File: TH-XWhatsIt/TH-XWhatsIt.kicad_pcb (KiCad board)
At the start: 2 copper layers, 145.3 x 129.6 mm, 32 parts, among them J1 MODEL F, J2 EXPANSION, J3 EXPANSION HEADER, J4 EXPANSION BEAMSPRING, J5 BEAMSPRING CONNECTOR, J6 EXPANSION BEAMSPRING, J7 EXPANSION DISPLAYWRITER, J8 DISPLAYWRITER CONNECTOR, J9 EXPANSION DISPLAYWRITER, U1 MCP4921-EP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

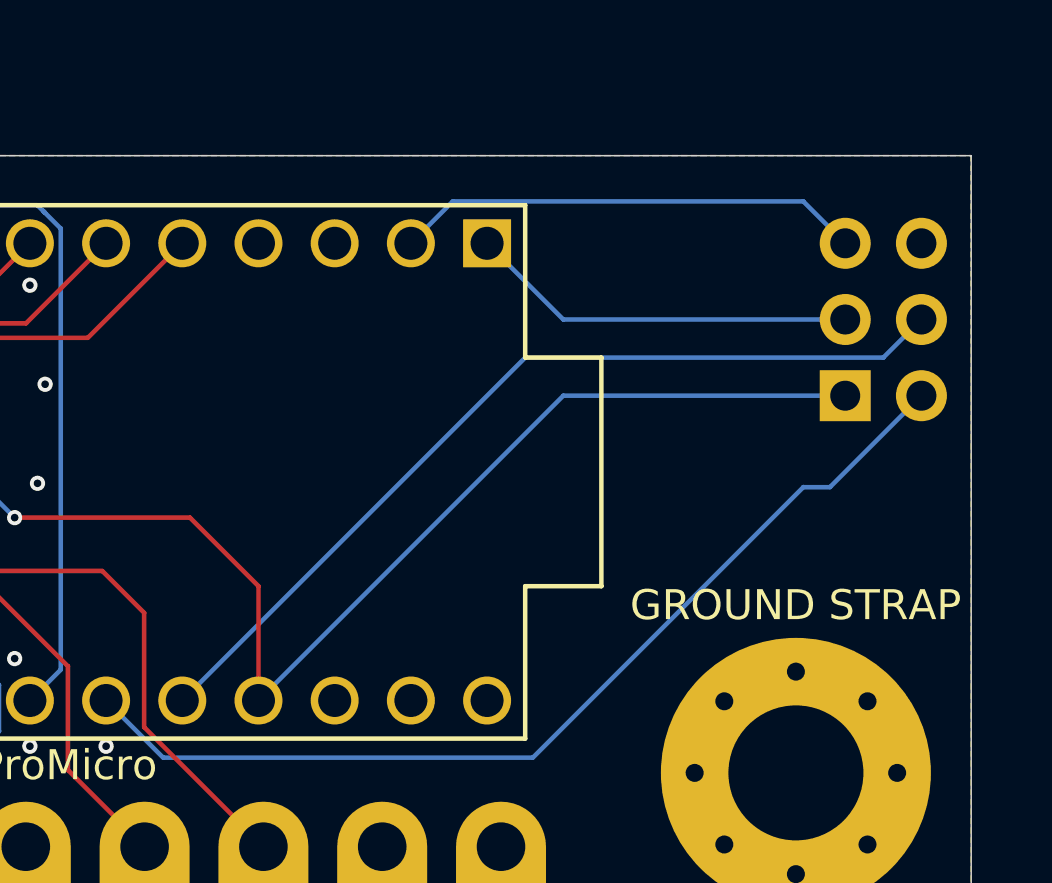
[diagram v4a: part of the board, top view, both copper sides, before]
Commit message: Added pads for easily shorting reset with a screwdriver
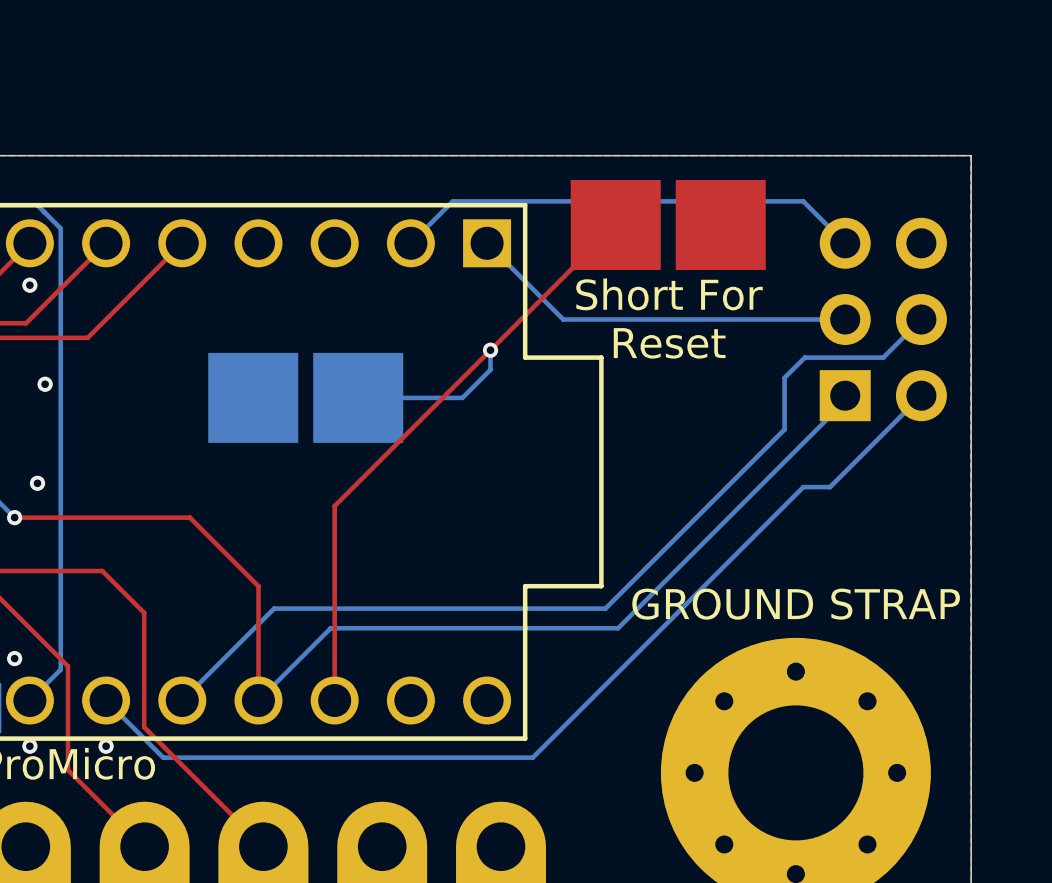
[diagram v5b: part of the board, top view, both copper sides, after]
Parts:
- added SW1: SW_Push, TH-XWhatsIt:PadsToShort, F.Cu at (165.9, 127.8)
- added SW2: SW_Push, TH-XWhatsIt:PadsToShort, B.Cu at (153.8, 133.6)
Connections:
- U5 pad 22: Net-(U5-Pad22) -> RST
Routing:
- net RST: track 0.00 -> 25.2 mm, vias 0 -> 1
- net HEADER4: track 29.9 -> 30.9 mm
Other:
- board text added: "Short For Reset"
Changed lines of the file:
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@@
   (general
     (thickness 1.6)
-    (drawings 31)
-    (tracks 1460)
+    (drawings 33)
+    (tracks 1473)
     (zones 0)
-    (modules 32)
+    (modules 34)
     (nets 132)
   )
@@
   )
   (layers
-    (0 F.Cu signal)
+    (0 F.Cu signal hide)
     (31 B.Cu signal)
     (32 B.Adhes user hide)
@@
     (34 B.Paste user hide)
     (35 F.Paste user hide)
-    (36 B.SilkS user hide)
-    (37 F.SilkS user)
+    (36 B.SilkS user)
+    (37 F.SilkS user hide)
     (38 B.Mask user hide)
     (39 F.Mask user hide)
@@
   (net 127 "Net-(J9-Pad3)")
   (net 128 "Net-(U5-Pad24)")
-  (net 129 "Net-(U5-Pad22)")
-  (net 130 "Net-(U7-Pad9)")
-  (net 131 "Net-(J4-Pad28)")
+  (net 129 "Net-(U7-Pad9)")
+  (net 130 "Net-(J4-Pad28)")
+  (net 131 RST)
   (net_class Default "This is the default net class."
     (clearance 0.1524)
@@
     (add_net "Net-(J9-Pad9)")
     (add_net "Net-(R4-Pad2)")
-    (add_net "Net-(U5-Pad22)")
     (add_net "Net-(U5-Pad24)")
     (add_net "Net-(U7-Pad9)")
@@
     (add_net ROW7)
     (add_net ROW8)
+    (add_net RST)
     (add_net SENSE1)
     (add_net SENSE2)
@@
     (add_net ~SELECTDAC)
   )
+  (module TH-XWhatsIt:PadsToShort (layer B.Cu)
+    (at 153.8478 133.5913 180)
+    (fp_text reference SW2 (at 0 -0.5) (layer B.SilkS) hide
+      (effects (font (size 1 1) (thickness 0.15)) (justify mirror))
+    )
+    (fp_text value SW_Push (at 0 0.5) (layer B.Fab) hide
+      (effects (font (size 1 1) (thickness 0.15)) (justify mirror))
+    )
+    (pad 2 smd rect (at 1.75 -2.88 180) (size 3 3) (layers B.Cu B.Paste B.Mask)
+      (net 48 GNDA))
+    (pad 1 smd rect (at -1.75 -2.88 180) (size 3 3) (layers B.Cu B.Paste B.Mask)
+      (net 131 RST))
+  )
+  (module TH-XWhatsIt:PadsToShort (layer F.Cu)
+    (at 165.93058 127.82804)
+    (fp_text reference SW1 (at -0.0381 5.37972) (layer F.SilkS) hide
+      (effects (font (size 1 1) (thickness 0.15)))
+    )
+    (fp_text value SW_Push (at 0 -0.5) (layer F.Fab)
+      (effects (font (size 1 1) (thickness 0.15)))
+    )
+    (pad 2 smd rect (at 1.75 2.88) (size 3 3) (layers F.Cu F.Paste F.Mask)
+      (net 48 GNDA))
+    (pad 1 smd rect (at -1.75 2.88) (size 3 3) (layers F.Cu F.Paste F.Mask)
+      (net 131 RST))
+  )
   (module Resistor_SMD:R_Array_Convex_4x0603 (layer F.Cu)
     (at 59.436 146.304 270)
@@
       (effects (font (size 1 1) (thickness 0.15)))
     )
-    (fp_text user %R (at 0 0) (layer F.Fab)
-      (effects (font (size 0.5 0.5) (thickness 0.075)))
-    )
     (fp_line (start -0.8 -1.6) (end 0.8 -1.6) (layer F.Fab) (width 0.1))
     (fp_line (start 0.8 -1.6) (end 0.8 1.6) (layer F.Fab) (width 0.1))
@@
     (fp_line (start 1.55 1.85) (end 1.55 -1.85) (layer F.CrtYd) (width 0.05))
     (fp_line (start 1.55 1.85) (end -1.55 1.85) (layer F.CrtYd) (width 0.05))
+    (fp_text user %R (at 0 0) (layer F.Fab)
+      (effects (font (size 0.5 0.5) (thickness 0.075)))
+    )
     (pad 5 smd rect (at 0.9 1.2 270) (size 0.8 0.5) (layers F.Cu F.Paste F.Mask)
       (net 24 SENSE1))
@@
       (effects (font (size 1 1) (thickness 0.15)))
     )
-    (fp_text user %R (at 0 0) (layer F.Fab)
-      (effects (font (size 0.5 0.5) (thickness 0.075)))
-    )
     (fp_line (start -0.8 -1.6) (end 0.8 -1.6) (layer F.Fab) (width 0.1))
     (fp_line (start 0.8 -1.6) (end 0.8 1.6) (layer F.Fab) (width 0.1))
@@
     (fp_line (start 1.55 1.85) (end 1.55 -1.85) (layer F.CrtYd) (width 0.05))
     (fp_line (start 1.55 1.85) (end -1.55 1.85) (layer F.CrtYd) (width 0.05))
+    (fp_text user %R (at 0 0) (layer F.Fab)
+      (effects (font (size 0.5 0.5) (thickness 0.075)))
+    )
     (pad 5 smd rect (at 0.9 1.2 270) (size 0.8 0.5) (layers F.Cu F.Paste F.Mask)
       (net 28 SENSE5))
@@
       (net 48 GNDA))
     (pad 22 thru_hole circle (at -8.89 -7.62 180) (size 1.6 1.6) (drill 1.1) (layers *.Cu *.Mask F.SilkS)
-      (net 129 "Net-(U5-Pad22)"))
+      (net 131 RST))
     (pad 21 thru_hole circle (at -6.35 -7.62 180) (size 1.6 1.6) (drill 1.1) (layers *.Cu *.Mask F.SilkS)
       (net 49 +5VA))
@@
       (net 50 "/beamspring plugboard/BSGROUND"))
     (pad 28 thru_hole oval (at 49.5 -2.54) (size 3 5.5) (drill 1.62 (offset 0 1.25)) (layers *.Cu *.Mask)
-      (net 131 "Net-(J4-Pad28)"))
+      (net 130 "Net-(J4-Pad28)"))
     (pad 27 thru_hole oval (at 45.54 -2.54) (size 3 5.5) (drill 1.62 (offset 0 1.25)) (layers *.Cu *.Mask)
       (net 59 "/beamspring plugboard/BSCOL15"))
@@
       (net 50 "/beamspring plugboard/BSGROUND"))
     (pad 28 thru_hole circle (at 49.5 0) (size 3 3) (drill 1.6) (layers *.Cu *.Mask)
-      (net 131 "Net-(J4-Pad28)"))
+      (net 130 "Net-(J4-Pad28)"))
     (pad 27 thru_hole circle (at 45.54 0) (size 3 3) (drill 1.6) (layers *.Cu *.Mask)
       (net 59 "/beamspring plugboard/BSCOL15"))
@@
       (net 49 +5VA))
     (pad 9 smd roundrect (at 2.475 4.445 90) (size 1.95 0.6) (layers F.Cu F.Paste F.Mask) (roundrect_rratio 0.25)
-      (net 130 "Net-(U7-Pad9)"))
+      (net 129 "Net-(U7-Pad9)"))
     (pad 8 smd roundrect (at -2.475 4.445 90) (size 1.95 0.6) (layers F.Cu F.Paste F.Mask) (roundrect_rratio 0.25)
       (net 48 GNDA))
@@
     )
   )
+  (gr_text "Short For\nReset" (at 153.75636 140.20546) (layer B.SilkS)
+    (effects (font (size 1 1) (thickness 0.15)) (justify mirror))
+  )
+  (gr_text "Short For\nReset" (at 165.92804 133.87578) (layer F.SilkS)
+    (effects (font (size 1 1) (thickness 0.15)))
+  )
   (gr_line (start 129.653 63.555) (end 162.246 63.555) (layer Edge.Cuts) (width 0.05))
   (gr_line (start 162.246 24.391) (end 162.246 44.015) (layer Edge.Cuts) (width 0.05))
@@
   (segment (start 87.057 135.763) (end 87.757 136.463) (width 0.1524) (layer F.Cu) (net 49) (status 20))
   (segment (start 86.187 135.763) (end 87.057 135.763) (width 0.1524) (layer F.Cu) (net 49) (status 10))
-  (segment (start 162.433 136.398) (end 171.831 136.398) (width 0.1524) (layer B.Cu) (net 49) (status 20))
-  (segment (start 152.273 146.558) (end 162.433 136.398) (width 0.1524) (layer B.Cu) (net 49) (status 10))
   (via (at 125.73 135.001) (size 0.508) (drill 0.254) (layers F.Cu B.Cu) (net 49))
   (segment (start 125.73 136.463) (end 125.73 135.001) (width 0.1524) (layer F.Cu) (net 49) (status 10))
@@
   (segment (start 131.32308 136.652) (end 140.335 136.652) (width 0.1524) (layer B.Cu) (net 49))
   (segment (start 128.06172 135.32612) (end 129.9972 135.32612) (width 0.1524) (layer B.Cu) (net 49))
+  (segment (start 171.831 136.398) (end 171.831 136.57834) (width 0.1524) (layer B.Cu) (net 49))
+  (segment (start 171.831 136.57834) (end 164.25926 144.15008) (width 0.1524) (layer B.Cu) (net 49))
+  (segment (start 154.68092 144.15008) (end 152.273 146.558) (width 0.1524) (layer B.Cu) (net 49))
+  (segment (start 164.25926 144.15008) (end 154.68092 144.15008) (width 0.1524) (layer B.Cu) (net 49))
   (via (at 45.419 64.262) (size 0.508) (drill 0.254) (layers F.Cu B.Cu) (net 50))
   (segment (start 144.517 28.544) (end 144.517 36.464) (width 0.1524) (layer B.Cu) (net 50) (status 30))
@@
   (segment (start 162.433 133.858) (end 159.893 131.318) (width 0.1524) (layer B.Cu) (net 101) (status 20))
   (segment (start 171.831 133.858) (end 162.433 133.858) (width 0.1524) (layer B.Cu) (net 101) (status 10))
-  (segment (start 149.733 146.558) (end 161.163 135.128) (width 0.1524) (layer B.Cu) (net 102) (status 10))
   (segment (start 173.101 135.128) (end 174.371 133.858) (width 0.1524) (layer B.Cu) (net 102) (status 20))
-  (segment (start 161.163 135.128) (end 173.101 135.128) (width 0.1524) (layer B.Cu) (net 102))
+  (segment (start 173.101 135.128) (end 170.4848 135.128) (width 0.1524) (layer B.Cu) (net 102))
+  (segment (start 170.4848 135.128) (end 169.80916 135.80364) (width 0.1524) (layer B.Cu) (net 102))
+  (segment (start 169.80916 135.80364) (end 169.80916 137.52576) (width 0.1524) (layer B.Cu) (net 102))
+  (segment (start 169.80916 137.52576) (end 163.84016 143.49476) (width 0.1524) (layer B.Cu) (net 102))
+  (segment (start 152.79624 143.49476) (end 149.733 146.558) (width 0.1524) (layer B.Cu) (net 102))
+  (segment (start 163.84016 143.49476) (end 152.79624 143.49476) (width 0.1524) (layer B.Cu) (net 102))
   (segment (start 95.377 141.413) (end 95.377 139.827) (width 0.1524) (layer F.Cu) (net 103) (status 10))
   (segment (start 95.377 139.827) (end 97.409 137.795) (width 0.1524) (layer F.Cu) (net 103))
@@
   (segment (start 69.56806 146.431) (end 67.945 146.431) (width 0.1524) (layer B.Cu) (net 111))
   (segment (start 71.50354 144.49552) (end 69.56806 146.431) (width 0.1524) (layer B.Cu) (net 111))
+  (segment (start 154.813 140.07562) (end 160.00715 134.88147) (width 0.1524) (layer F.Cu) (net 131))
+  (segment (start 154.813 146.558) (end 154.813 140.07562) (width 0.1524) (layer F.Cu) (net 131))
+  (segment (start 160.00715 134.88147) (end 164.18058 130.70804) (width 0.1524) (layer F.Cu) (net 131))
+  (via (at 160.00715 134.88147) (size 0.508) (drill 0.254) (layers F.Cu B.Cu) (net 131))
+  (segment (start 160.00715 134.88147) (end 160.00715 135.53455) (width 0.1524) (layer B.Cu) (net 131))
+  (segment (start 159.0704 136.4713) (end 155.5978 136.4713) (width 0.1524) (layer B.Cu) (net 131))
+  (segment (start 160.00715 135.53455) (end 159.0704 136.4713) (width 0.1524) (layer B.Cu) (net 131))
   (zone (net 48) (net_name GNDA) (layer B.Cu) (hatch edge 0.508)
     (connect_pads (clearance 0.152))

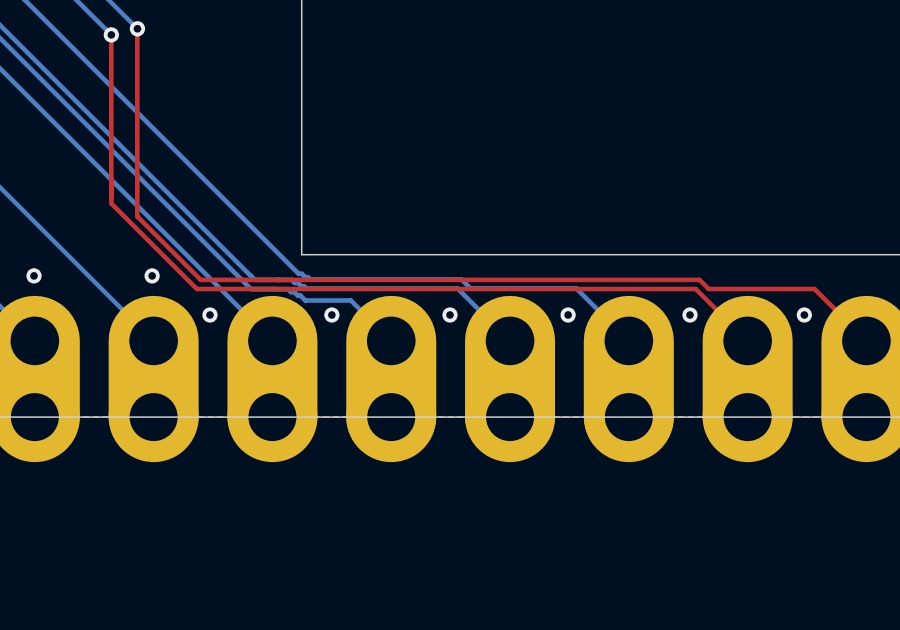
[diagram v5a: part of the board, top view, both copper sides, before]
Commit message: pcb: removed some useless vias
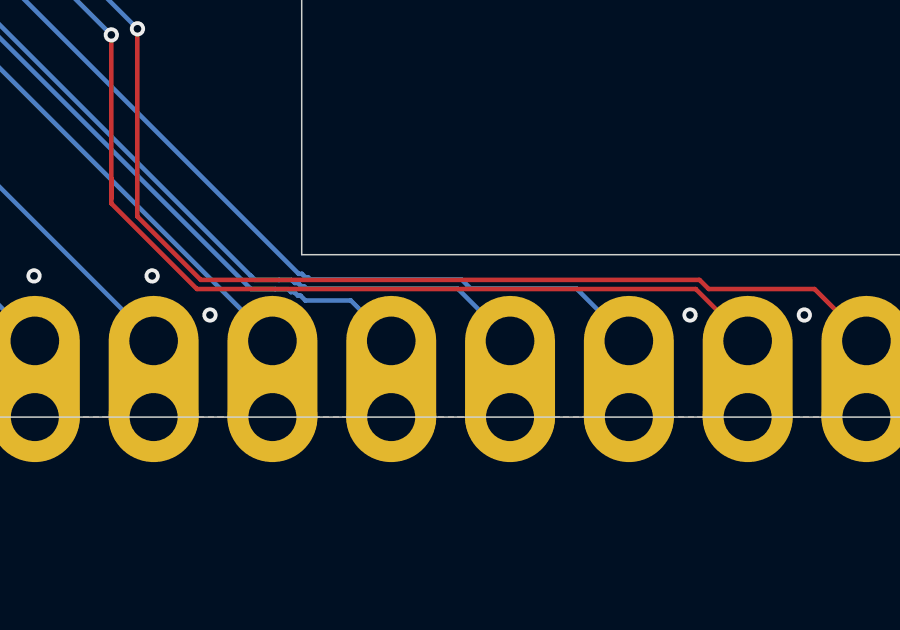
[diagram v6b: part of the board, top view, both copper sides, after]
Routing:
- net /beamspring plugboard/BSGROUND: vias 46 -> 43
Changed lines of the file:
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@@
     (thickness 1.6)
     (drawings 33)
-    (tracks 1473)
+    (tracks 1470)
     (zones 0)
     (modules 34)
@@
   )
   (layers
-    (0 F.Cu signal hide)
+    (0 F.Cu signal)
     (31 B.Cu signal)
     (32 B.Adhes user hide)
@@
   (via (at 124.667 64.262) (size 0.508) (drill 0.254) (layers F.Cu B.Cu) (net 50))
   (via (at 126.59486 65.56502) (size 0.508) (drill 0.254) (layers F.Cu B.Cu) (net 50))
-  (via (at 130.65886 65.56502) (size 0.508) (drill 0.254) (layers F.Cu B.Cu) (net 50))
-  (via (at 134.59586 65.56502) (size 0.508) (drill 0.254) (layers F.Cu B.Cu) (net 50))
-  (via (at 138.53286 65.56502) (size 0.508) (drill 0.254) (layers F.Cu B.Cu) (net 50))
   (via (at 142.59686 65.56502) (size 0.508) (drill 0.254) (layers F.Cu B.Cu) (net 50))
   (via (at 146.40686 65.56502) (size 0.508) (drill 0.254) (layers F.Cu B.Cu) (net 50))
